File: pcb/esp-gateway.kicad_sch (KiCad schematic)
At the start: 33 parts, among them J1 ESP-01, J10 JMP, J2 RF-TR, J3 RF-RX, J4 USB, J5 Conn_01x02, J6 Conn_01x02, J7 UART0, J8 Conn_01x02, J9 Conn_02x04_Counter_Clockwise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

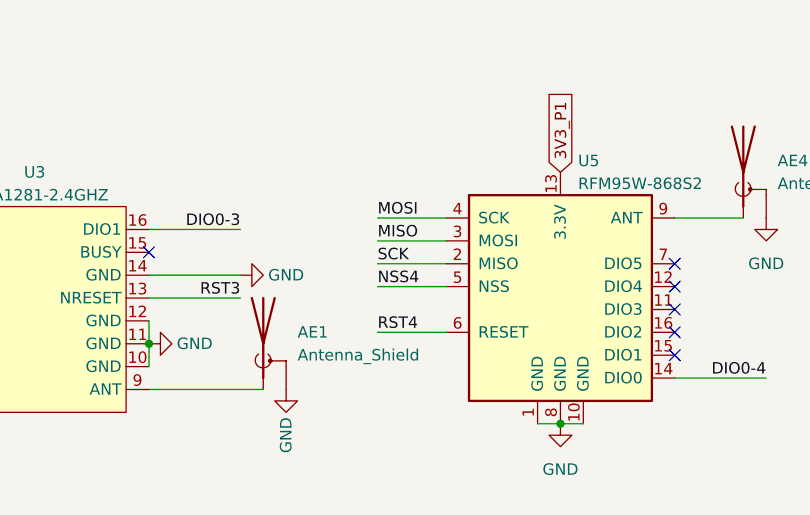
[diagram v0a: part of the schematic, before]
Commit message: fix rfm pinout
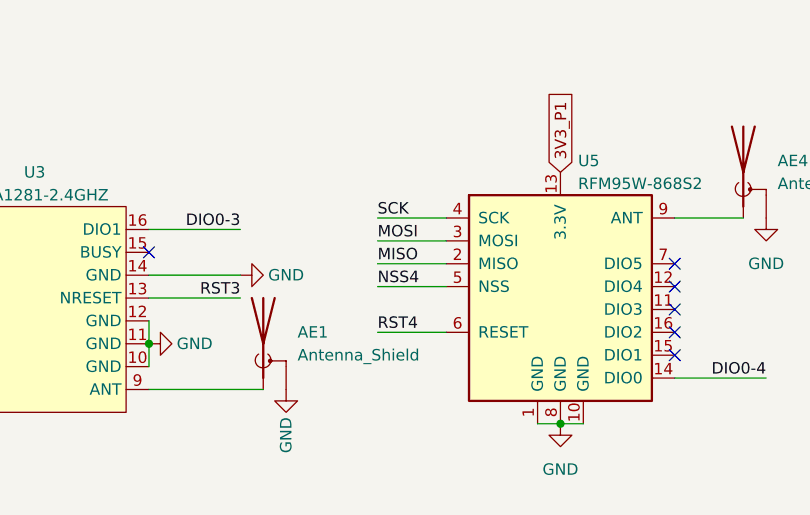
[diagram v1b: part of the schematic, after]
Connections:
- net MISO: now also U5.2 (MISO); no longer U5.3 (MOSI)
- net MOSI: now also U5.3 (MOSI); no longer U5.4 (SCK)
- net SCK: now also U5.4 (SCK); no longer U5.2 (MISO)
